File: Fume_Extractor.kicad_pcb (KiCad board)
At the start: 2 copper layers, 40 x 60 mm, 22 parts, among them J1 USB_B_Micro, J2 Conn_01x02, J3 Conn_01x02, U1 SP34063AEN, U2 TP4056

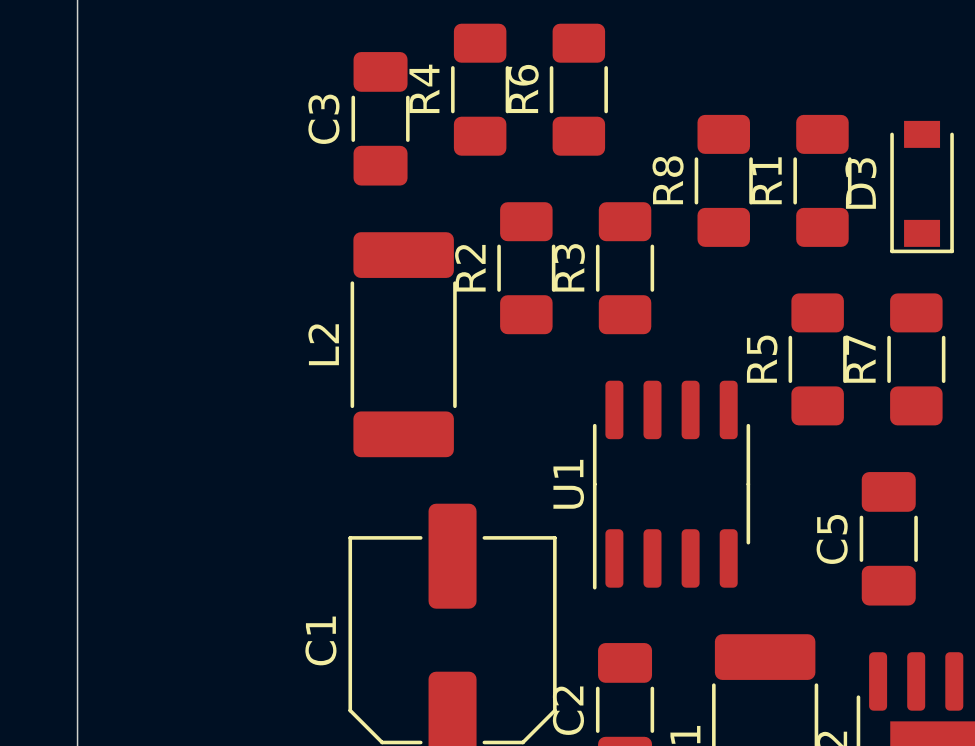
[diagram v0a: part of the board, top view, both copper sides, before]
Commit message: update schematic
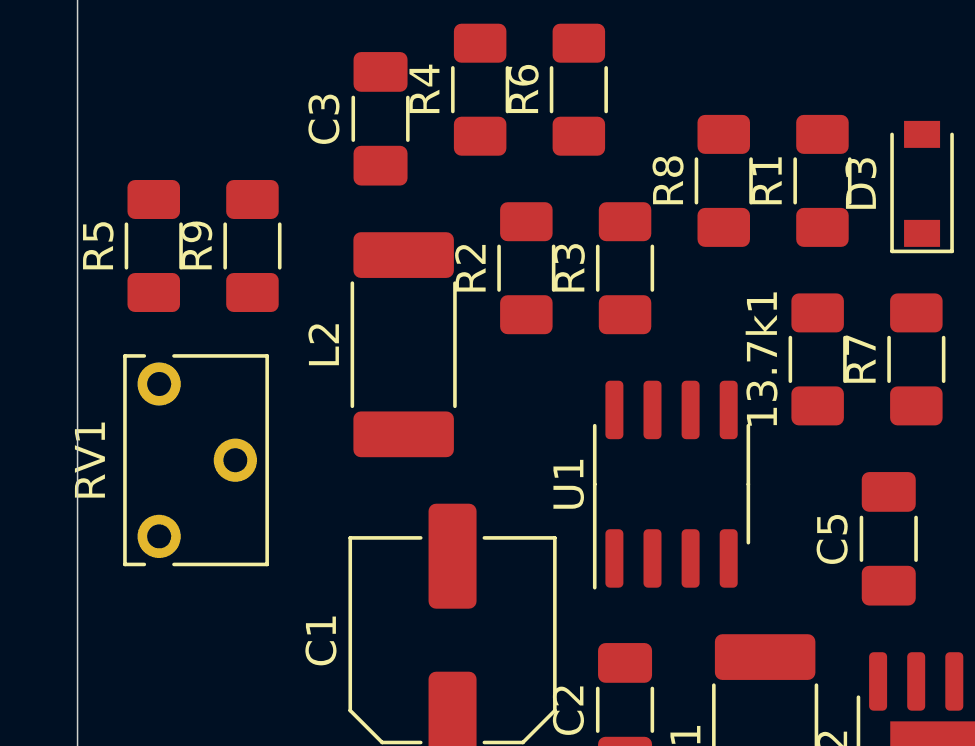
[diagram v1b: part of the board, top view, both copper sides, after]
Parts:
- added R5: 48k, Resistor_SMD:R_1206_3216Metric_Pad1.30x1.75mm_HandSolder, F.Cu at (2.54, 22.9)
- added R9: 508.064k, Resistor_SMD:R_1206_3216Metric_Pad1.30x1.75mm_HandSolder, F.Cu at (5.83, 22.9)
- added RV1: 500M, Potentiometer_THT:Potentiometer_Bourns_3266W_Vertical, F.Cu at (2.72, 27.5)
- R2: value R2 -> 0.22 R
- R7: value R1 -> 118k
- renumbered R5 to 13.7k1

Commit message: Major schematic and layout updates
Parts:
- removed 13.7k1: R2, Resistor_SMD:R_1206_3216Metric_Pad1.30x1.75mm_HandSolder
- removed C3: 1.5nF ±10% 50V X7R 1206, Capacitor_SMD:C_1206_3216Metric_Pad1.33x1.80mm_HandSolder
- removed C4: 330uF ±20% 50V, Capacitor_SMD:CP_Elec_10x12.5
- removed C5: 10uF, Capacitor_SMD:C_1206_3216Metric_Pad1.33x1.80mm_HandSolder
- added C7: 10uF, Capacitor_SMD:C_1206_3216Metric_Pad1.33x1.80mm_HandSolder, F.Cu at (27.5, 18.5)
- added C8: 100uF ±20% 50V, Capacitor_SMD:CP_Elec_8x10, F.Cu at (61.0, 13.0)
- added C9: 10uF, Capacitor_SMD:C_1206_3216Metric_Pad1.33x1.80mm_HandSolder, F.Cu at (21.5, 18.5)
- added D1: 40V 1A 450mV @ 1A, Diode_SMD:D_SOD-123, F.Cu at (52.0, 25.0)
- added D2: LED, Diode_SMD:D_1206_3216Metric_Pad1.42x1.75mm_HandSolder, F.Cu at (21.0, 0.00)
- added SW1: SW_SPDT, Fume_Extractor:Switch_SS-12D06L5, F.Cu at (40.0, -2.00)
- C1: value 100µF -> 100uF ±20% 50V; footprint Capacitor_SMD:CP_Elec_6.3x5.3 -> Capacitor_SMD:CP_Elec_8x10
- C2: value 10uF -> 1.5nF ±10% 50V X7R 1206
- C6: value 100uF ±20% 50V -> 330uF ±20% 50V; footprint Capacitor_SMD:CP_Elec_8x10 -> Capacitor_SMD:CP_Elec_10x12.5
- D3: value 40V 1A 450mV @ 1A -> LED; footprint Diode_SMD:D_SOD-123 -> Diode_SMD:D_1206_3216Metric_Pad1.42x1.75mm_HandSolder
- L1: value 150uH ±10% 6*8 Radial Inductor -> 150uH ±20% 1.42A 280mΩ; footprint Inductor_SMD:L_2512_6332Metric_Pad1.52x3.35mm_HandSolder -> Fume_Extractor:Inductor_SLH_12x12x8
- R1: value R1 -> 0.22 R
- R2: value 0.22 R -> 180R
- R3: value 10k -> 16k
- R4: value 180R -> 0R
- R5: value 48k -> 508.064k
- R6: value 10k -> 48k
- R7: value 118k -> 10k
- R8: value RProg -> 10k
- R9: value 508.064k -> 1.2 k
- RV1: value 500M -> 500k
- moved C6 44.8 mm to (62.0, 24.0), turned to 0 degrees
- moved L2 42.1 mm to (52.0, 17.0)
- moved J1 33.1 mm to (60.7, 4.00)
- moved RV1 31.3 mm to (28.0, 9.00)
- moved C2 25.7 mm to (10.0, 14.0), turned to 270 degrees
- moved L1 25.2 mm to (40.0, 21.1), turned to 180 degrees
- moved R5 24.7 mm to (22.9, 9.00), turned to 0 degrees
- moved R7 23.7 mm to (21.0, 4.00), turned to 0 degrees
- moved R9 23.0 mm to (28.5, 26.5)
- moved D3 20.8 mm to (27.0, 0.00), turned to 0 degrees
- moved U1 19.7 mm to (16.0, 11.5), turned to 0 degrees
- moved R2 19.6 mm to (15.5, 4.00), turned to 180 degrees
- moved J3 19.4 mm to (4.50, 23.5), turned to 270 degrees
- moved R8 17.6 mm to (27.0, 4.00), turned to 180 degrees
- moved U2 17.4 mm to (22.5, 23.5), turned to 180 degrees
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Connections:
- C1 pad 1: VCC -> VBATT
- C2 pad 1: +5V -> Net-(C2-Pad1)
- C6 pad 1: +12V -> Net-(C6-Pad1)
- D3 pad 1: Net-(C4-Pad1) -> Net-(D3-Pad1)
- J2 pad 1: VBATT -> Net-(J2-Pad1)
- J3 pad 1: +12V -> VBATT
- L1 pad 1: Net-(L1-Pad1) -> Net-(D1-Pad2)
- L1 pad 2: Net-(D3-Pad2) -> Net-(L1-Pad2)
- L2 pad 1: Net-(C4-Pad1) -> Net-(C6-Pad1)
- L2 pad 2: +12V -> +24V
- R1 pad 1: Net-(F2-Pad2) -> Net-(L1-Pad2)
- R1 pad 2: +5V -> VBATT
- R2 pad 1: Net-(L1-Pad1) -> Net-(R2-Pad1)
- R2 pad 2: VCC -> Net-(L1-Pad2)
- R3 pad 1: Net-(D1-Pad2) -> GND
- R3 pad 2: +5V -> Net-(R3-Pad2)
- R4 pad 2: Net-(L1-Pad1) -> Net-(R3-Pad2)
- R5 pad 1: Net-(R5-Pad1) -> Net-(R3-Pad2)
- R6 pad 1: Net-(D2-Pad2) -> Net-(R5-Pad2)
- R6 pad 2: +5V -> Net-(C6-Pad1)
- R7 pad 1: Net-(C4-Pad1) -> Net-(D2-Pad2)
- R7 pad 2: Net-(13.7k1-Pad2) -> +5V
- R8 pad 1: GND -> Net-(D3-Pad2)
- R8 pad 2: Net-(R8-Pad2) -> +5V
- R9 pad 1: Net-(R9-Pad1) -> GND
- R9 pad 2: Net-(R5-Pad1) -> Net-(R9-Pad2)
- RV1 pad 1: Net-(R5-Pad1) -> Net-(R5-Pad2)
- RV1 pad 2: Net-(R9-Pad1) -> Net-(R3-Pad2)
- RV1 pad 3: Net-(RV1-Pad3) -> Net-(R4-Pad1)
- U1 pad 1: Net-(D3-Pad2) -> Net-(D1-Pad2)
- U1 pad 3: Net-(C3-Pad1) -> Net-(C2-Pad1)
- U1 pad 5: Net-(13.7k1-Pad2) -> Net-(R3-Pad2)
- U1 pad 6: Net-(L1-Pad1) -> VBATT
- U1 pad 7: Net-(L1-Pad1) -> Net-(L1-Pad2)
- U1 pad 8: Net-(R4-Pad1) -> Net-(R2-Pad1)
- U2 pad 1: Net-(F2-Pad2) -> GND
- U2 pad 2: Net-(R8-Pad2) -> Net-(R9-Pad2)
- U2 pad 7: Net-(D2-Pad1) (its old number) -> Net-(D3-Pad1)
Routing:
- net +5V: track 0.00 -> 92.2 mm
- net Net-(C6-Pad1): track 0.00 -> 63.6 mm, vias 0 -> 2
- net Net-(D3-Pad1): track 0.00 -> 51.9 mm, vias 0 -> 2
- net Net-(D1-Pad2): track 0.00 -> 49.6 mm, vias 0 -> 2
- net Net-(L1-Pad2): track 0.00 -> 46.7 mm, vias 0 -> 4
- net Net-(D2-Pad1): track 0.00 -> 42.9 mm, vias 0 -> 2
- net Net-(J2-Pad1): track 0.00 -> 33.3 mm
- net VBATT: track 0.00 -> 31.9 mm
- net +24V: track 0.00 -> 27.1 mm
- net Net-(R3-Pad2): track 0.00 -> 24.3 mm
- net Net-(R5-Pad2): track 0.00 -> 15.3 mm, vias 0 -> 1
- net Net-(R2-Pad1): track 0.00 -> 9.19 mm
- net Net-(R4-Pad1): track 0.00 -> 5.74 mm
- net Net-(D3-Pad2): track 0.00 -> 4.03 mm
- net Net-(D2-Pad2): track 0.00 -> 4.03 mm
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- added copper zone on F.Cu, net GND
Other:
- board size 40 x 60 mm -> 78 x 40 mm
